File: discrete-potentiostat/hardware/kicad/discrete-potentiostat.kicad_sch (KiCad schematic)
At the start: 70 parts, among them J1 ELECTRODES, J2 SWD, U1 BQ51013BRHLR, U2 MIC5205-3.3YM5, U3 nRF52832-QFAA, U4 OPA2391DGKR, U5 REF35102QDBVR, U6 MCP73832T-2ACI/OT, Y1 32MHz 8pF 10ppm

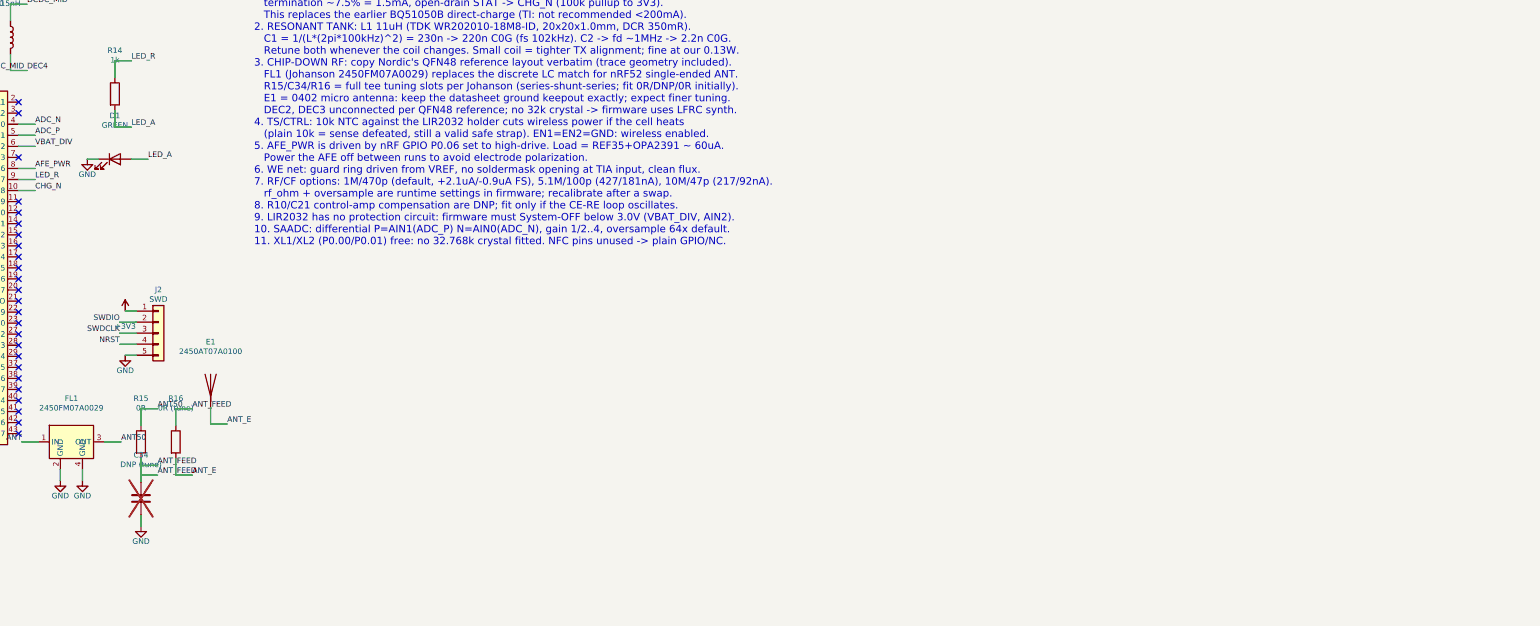
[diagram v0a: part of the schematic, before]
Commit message: Antenna tuning: switch tee to pi (shunt-series-shunt) per 2450AT07A0100 datasheet
The 0402 micro antenna's datasheet states non-eval PCBs will require a
pi network for proper resonance (eval board alone gets away with 0R).
Slots: C35 (DNP) - R15 (0R) - C34 (DNP). Also documents the keepout:
~5x3mm copper-free zone on all layers at the board corner; battery can
and Qi coil must stay out from under it. Netlist PASS.

Co-Authored-By: Claude Fable 5 <noreply@anthropic.com>
Claude-Session: https://claude.ai/code/session_01GUNJUwfGKqvkZFmTaLQRu3
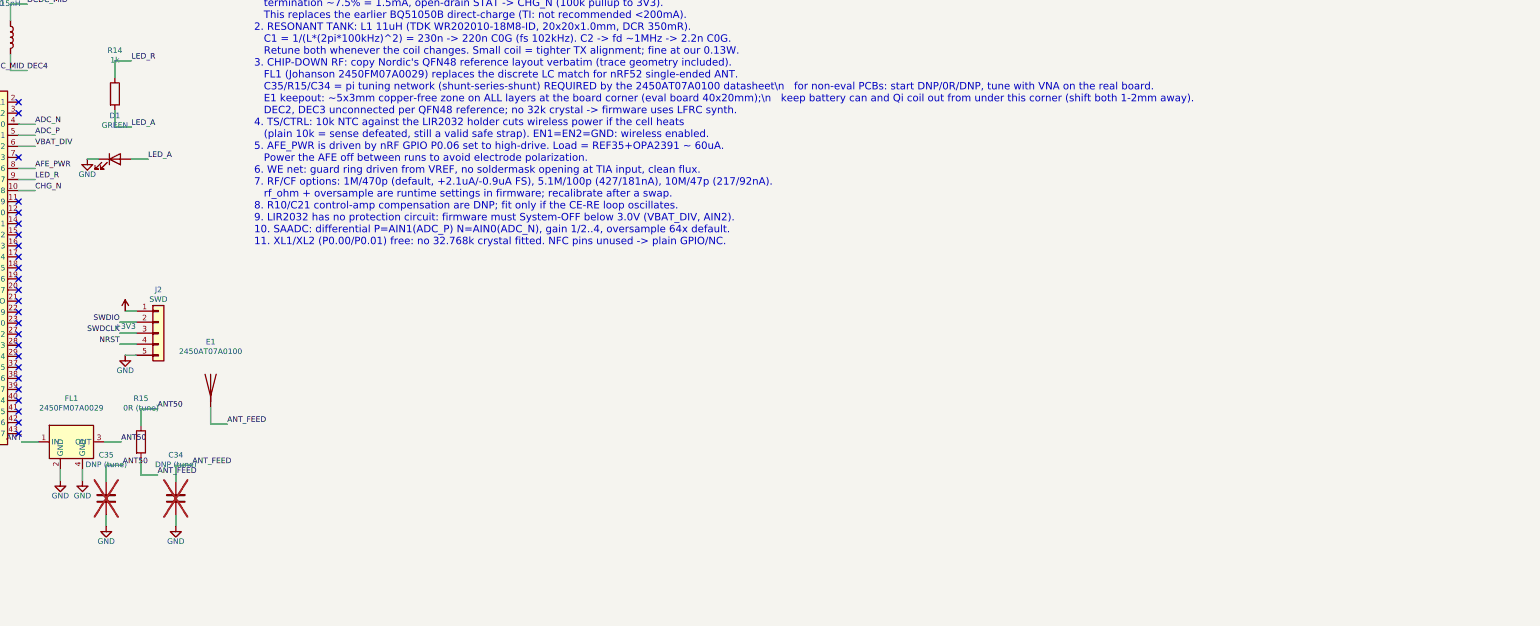
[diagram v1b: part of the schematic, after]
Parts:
- removed R16: 0R (tune), Resistor_SMD:R_0402_1005Metric, symbol Device:R
- added C35: DNP (tune), Capacitor_SMD:C_0402_1005Metric, symbol Device:C
- R15: value 0R -> 0R (tune)
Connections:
- net ANT_E is gone; now on net ANT_FEED: E1.1 (A)
- net ANT50: now also C35.1
- net GND: now also C35.2

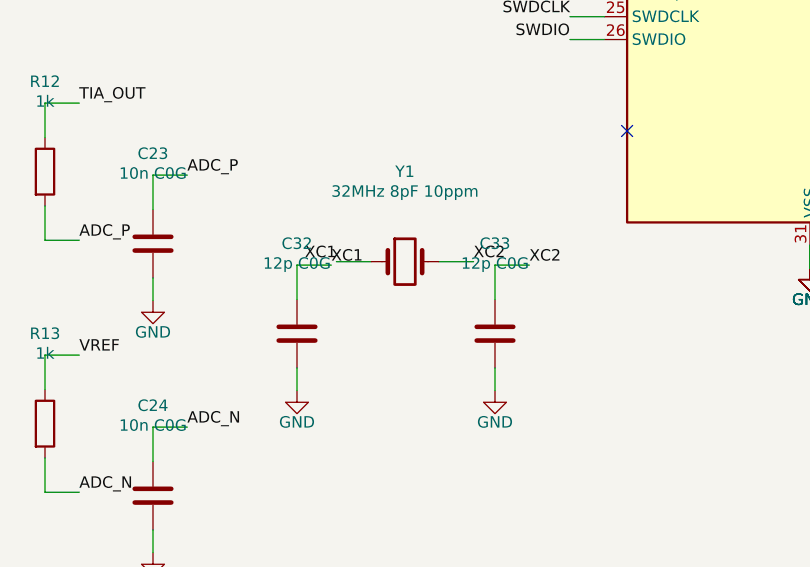
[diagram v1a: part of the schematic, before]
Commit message: Add PCB layout: 24x22mm 4-layer, placement complete and verified
Generated with the pcbnew API from the schematic netlist (all 70
footprints, 77 nets assigned). Verified zero courtyard overlaps and zero
board-edge violations via generator/check_pcb.py after an automated
legalization pass.

- Floorplan: Qi charger top-left (coil lead pads on left edge), RF corner
  top-right with the 5x3mm all-layer antenna keepout (rule area: no pours
  no vias, feed track allowed), nRF52832+crystal right-center, AFE bottom
  left with electrode header, MCP73832/LED/SWD bottom-right, tab-welded
  LIR2032 pads centered on the back
- RF feed pre-routed: ANT -> 2450FM07A0029 -> pi slots -> chip antenna
- GND pours on all 4 layers; battery: Keystone 3034 retainer is 27mm wide
  and does not fit -> solder-tab cell pads instead (BOM updated)
- Remaining for fab: interactive routing (ratsnest ready), DRC in KiCad 8+,
  50-ohm width vs final stackup, antenna VNA tuning

Co-Authored-By: Claude Fable 5 <noreply@anthropic.com>
Claude-Session: https://claude.ai/code/session_01GUNJUwfGKqvkZFmTaLQRu3
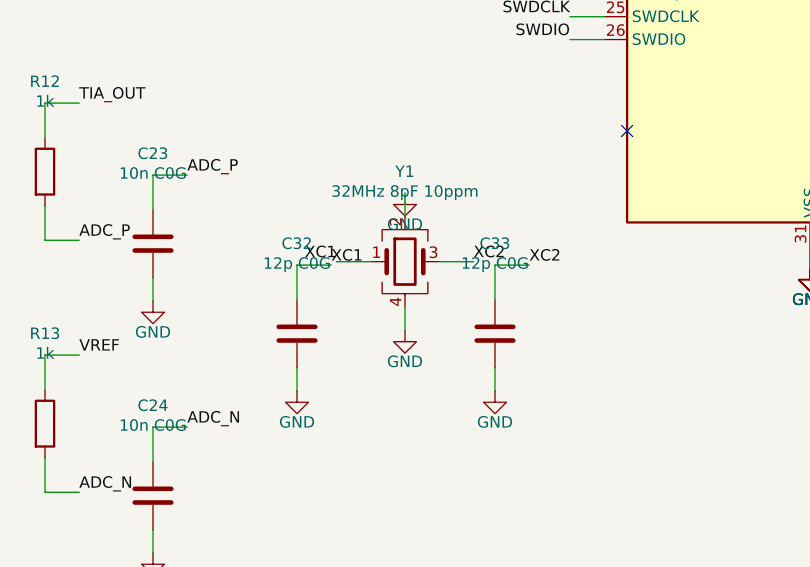
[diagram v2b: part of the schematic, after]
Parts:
- removed Y1: 32MHz 8pF 10ppm, Crystal:Crystal_SMD_3225-4Pin_3.2x2.5mm, symbol Device:Crystal
- added Y1: 32MHz 8pF 10ppm, Crystal:Crystal_SMD_3225-4Pin_3.2x2.5mm, symbol Device:Crystal_GND24
- BT1: footprint Battery:BT_Keystone_3034_1x2032 -> Battery:BatteryHolder_Keystone_3034_1x20mm
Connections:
- net GND: now also Y1.2, Y1.4
- net XC1: now also Y1.1
- net XC2: now also Y1.3

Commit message: 6-layer PCB + solder-pad connectors: auto-routing reaches ~92%
Per user decisions: (1) J1/J2 pin headers replaced with 1.0mm round
solder pads (1.8mm pitch) for direct wire soldering - also removes THT
barrels from inner layers; (2) board upgraded 4 -> 6 layers
(L1 sig/RF, L2 GND, L3/L4 routing, L5 GND, L6 sig+battery pads).

Router upgraded to 4 routing layers with through-vias, DRC-driven todo
override for RESUME runs, self-rip protection for large nets, and design
rules baked into generation (0.09/0.09, via 0.4/0.2). Result: unrouted
links 20 (4-layer) -> 8 (6-layer); 7 clearance items; finish guide in the
README (KiCad push-and-shove, ~30min). DRC report refreshed.

Co-Authored-By: Claude Fable 5 <noreply@anthropic.com>
Claude-Session: https://claude.ai/code/session_01GUNJUwfGKqvkZFmTaLQRu3
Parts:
- J1: footprint Connector_PinHeader_2.54mm:PinHeader_1x03_P2.54mm_Vertical -> pstat:SolderPads_1x03_D1.0mm
- J2: footprint Connector_PinHeader_1.27mm:PinHeader_1x05_P1.27mm_Vertical -> pstat:SolderPads_1x05_D1.0mm

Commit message: Swap op amp to LPV802 (nanopower) per user request
LPV802DGKR: 320nA/ch, 0.1pA input bias, 8kHz GBW, VSSOP-8 — same package
and standard dual pinout as the OPA2391 it replaces, so the PCB keeps its
routing (value updated in place). AFE rail drops to ~2uA total.

Trade-off documented: +/-3.5mV max offset -> +/-3.5nA fixed TIA offset at
RF=1M, removed by the existing zero-calibration step; pin-compatible
LPV812 (+/-0.3mV) noted as the precision upgrade. Netlist re-verified.

Co-Authored-By: Claude Fable 5 <noreply@anthropic.com>
Claude-Session: https://claude.ai/code/session_01GUNJUwfGKqvkZFmTaLQRu3
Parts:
- removed U4: OPA2391DGKR, Package_SO:VSSOP-8_3.0x3.0mm_P0.65mm, symbol pstat:OPA2391DGKR
- added U4: OPA2391DGKR, Package_SO:VSSOP-8_3.0x3.0mm_P0.65mm, symbol pstat:LPV802DGKR
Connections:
- net AFE_PWR: now also U4.8 (V+)
- net CE_AMP: now also U4.1 (OUT_A)
- net GND: now also U4.4 (V-)
- net RE: now also U4.2 (-IN_A)
- net TIA_OUT: now also U4.6 (-IN_B), U4.7 (OUT_B)
- net VBIAS: now also U4.3 (+IN_A)
- net VREF: now also U4.5 (+IN_B)

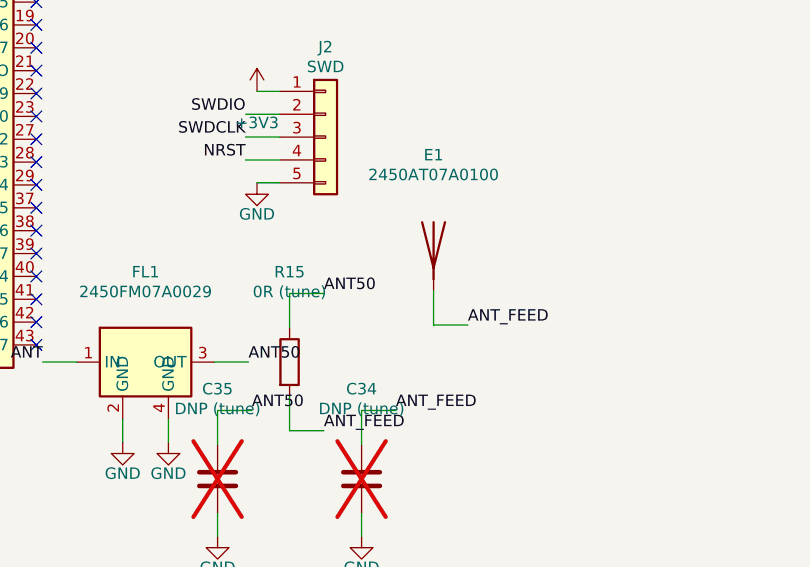
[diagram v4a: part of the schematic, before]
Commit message: Fix E1 antenna to datasheet-true 4-terminal land pattern (GND connected)
Johanson 2450AT07A0100 datasheet (36S0021A Rev 4.1) defines 4 terminals:
1/4 = Feed, 2/3 = GND. Previous footprint was a wrong 2-pad guess with
the GND end floating.

- gen_pcb.py: 4-pad footprint (0.3x0.25 pads, rows +-0.3 along L,
  columns +-0.175 across W per eval-board land pattern); E1 moved to
  (19.4, 0.95) rot 270 - vertical edge mount, GND row toward top edge;
  parametric feed bridge to R15.2 and 0.3mm GND strip into left F pour
- gen_sch.py: custom 4-pin antenna symbol (1/4 ANT_FEED, 2/3 GND);
  netlist check PASS (47 nets)
- Board file: live surgery applied (new E1 + feed bridge + GND strip,
  old 2-pad E1 and stub removed); DRC re-verified - zero copper
  violations (unconnected 0, clearance 0)
- Schematic/PDFs regenerated; bom.md and kicad/README.md updated

Co-Authored-By: Claude Fable 5 <noreply@anthropic.com>
Claude-Session: https://claude.ai/code/session_01GUNJUwfGKqvkZFmTaLQRu3
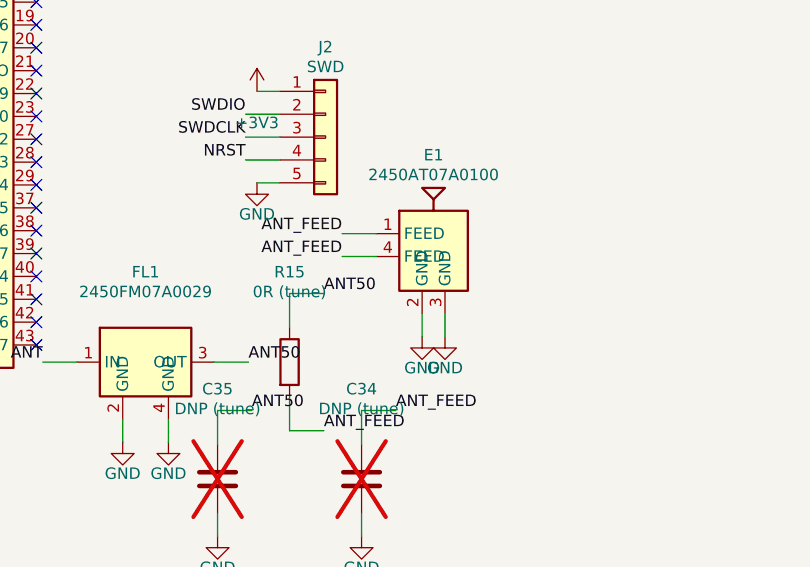
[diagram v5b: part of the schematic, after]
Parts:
- removed E1: 2450AT07A0100, pstat:Johanson_2450AT07A0100, symbol Device:Antenna
- added E1: 2450AT07A0100, pstat:Johanson_2450AT07A0100, symbol pstat:2450AT07A0100
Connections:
- net ANT_FEED: now also E1.1 (FEED), E1.4 (FEED)
- net GND: now also E1.2 (GND), E1.3 (GND)
